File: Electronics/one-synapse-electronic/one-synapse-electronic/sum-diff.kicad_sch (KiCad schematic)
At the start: 25 parts, among them J2 Axon, J3 Axon, U2 MCP6004

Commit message: WIP
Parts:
- J2, J3: footprint (none) -> Connector_PinSocket_2.54mm:PinSocket_1x08_P2.54mm_Vertical
- U2: footprint (none) -> Package_SO:HTSSOP-14-1EP_4.4x5mm_P0.65mm_EP3.4x5mm_Mask3x3.1mm
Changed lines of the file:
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@@
       (effects (font (size 1.27 1.27)))
     )
-    (property "Footprint" "" (at 151.13 120.65 0)
+    (property "Footprint" "Package_SO:HTSSOP-14-1EP_4.4x5mm_P0.65mm_EP3.4x5mm_Mask3x3.1mm" (at 151.13 120.65 0)
       (effects (font (size 1.27 1.27)) hide)
     )
@@
       (effects (font (size 1.27 1.27)))
     )
-    (property "Footprint" "" (at 179.07 54.61 0)
+    (property "Footprint" "Package_SO:HTSSOP-14-1EP_4.4x5mm_P0.65mm_EP3.4x5mm_Mask3x3.1mm" (at 179.07 54.61 0)
       (effects (font (size 1.27 1.27)) hide)
     )
@@
       (effects (font (size 1.27 1.27)) (justify left))
     )
-    (property "Footprint" "" (at 214.63 67.31 0)
+    (property "Footprint" "Connector_PinSocket_2.54mm:PinSocket_1x08_P2.54mm_Vertical" (at 214.63 67.31 0)
       (effects (font (size 1.27 1.27)) hide)
     )
@@
       (effects (font (size 1.27 1.27)))
     )
-    (property "Footprint" "" (at 151.13 106.68 0)
+    (property "Footprint" "Package_SO:HTSSOP-14-1EP_4.4x5mm_P0.65mm_EP3.4x5mm_Mask3x3.1mm" (at 151.13 106.68 0)
       (effects (font (size 1.27 1.27)) hide)
     )
@@
       (effects (font (size 1.27 1.27)))
     )
-    (property "Footprint" "" (at 151.13 138.43 0)
+    (property "Footprint" "Package_SO:HTSSOP-14-1EP_4.4x5mm_P0.65mm_EP3.4x5mm_Mask3x3.1mm" (at 151.13 138.43 0)
       (effects (font (size 1.27 1.27)) hide)
     )
@@
       (effects (font (size 1.27 1.27)) (justify left))
     )
-    (property "Footprint" "" (at 214.63 44.45 0)
+    (property "Footprint" "Connector_PinSocket_2.54mm:PinSocket_1x08_P2.54mm_Vertical" (at 214.63 44.45 0)
       (effects (font (size 1.27 1.27)) hide)
     )
@@
       (effects (font (size 1.27 1.27)))
     )
-    (property "Footprint" "" (at 151.13 52.07 0)
-      (effects (font (size 1.27 1.27)) hide)
-    )
+    (property "Footprint" "Package_SO:HTSSOP-14-1EP_4.4x5mm_P0.65mm_EP3.4x5mm_Mask3x3.1mm" (at 151.13 52.07 0)
+      (effects (font (size 1.27 1.27)) hide)
+    )

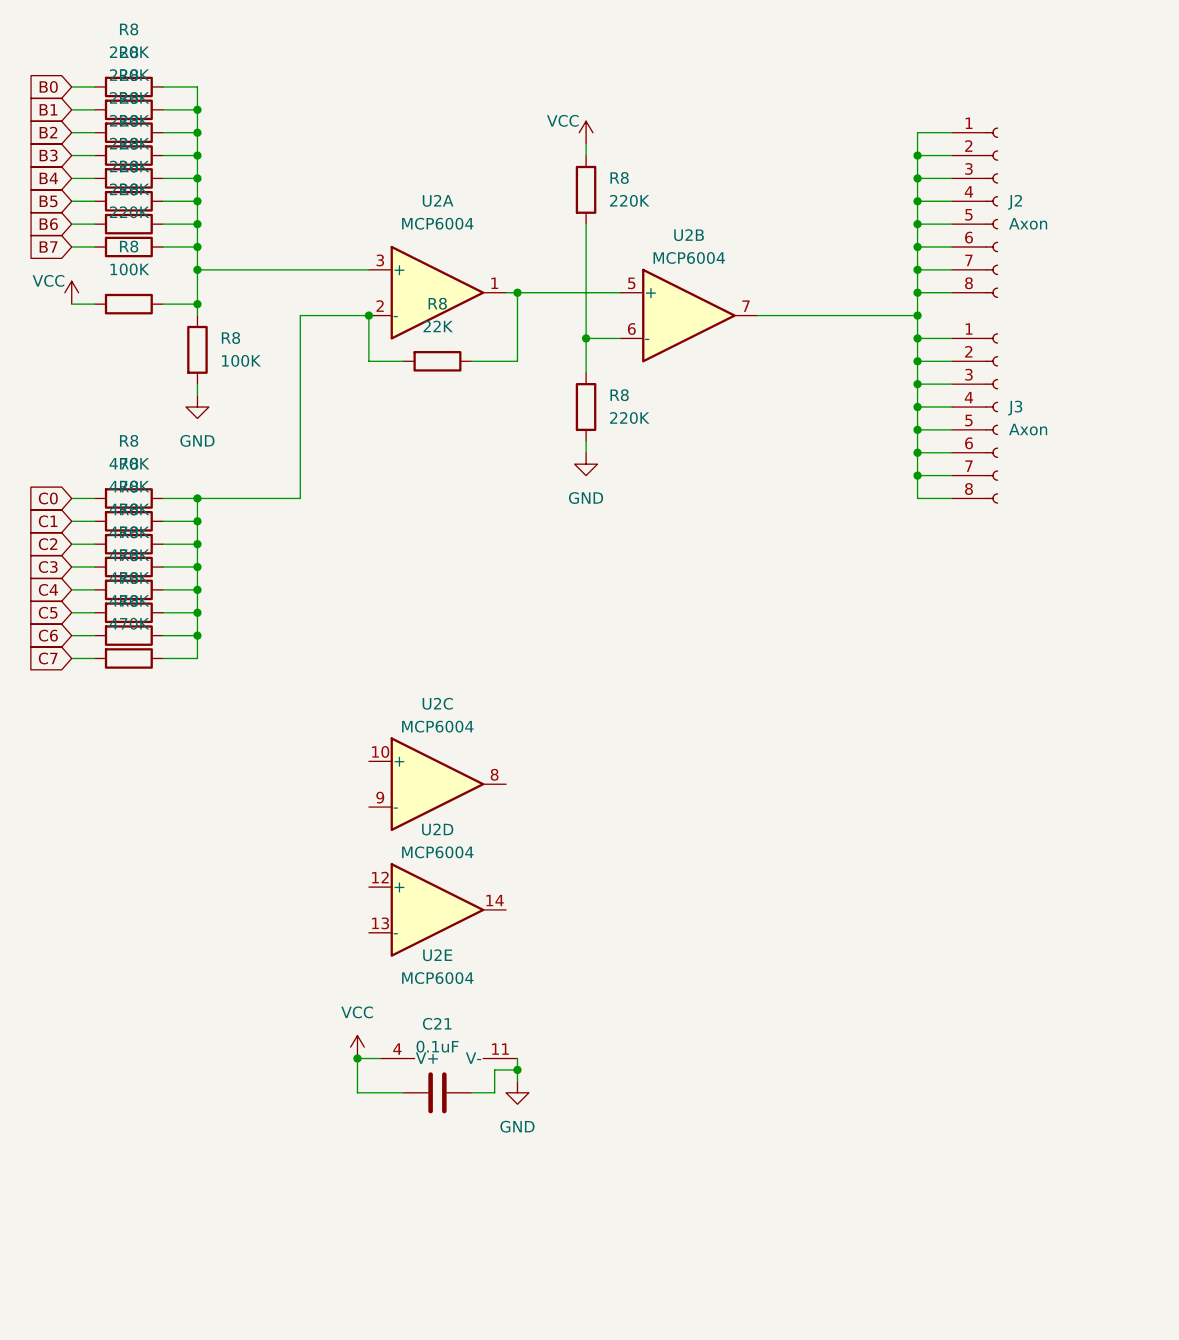
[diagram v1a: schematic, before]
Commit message: WIP. Added combiner i/o.
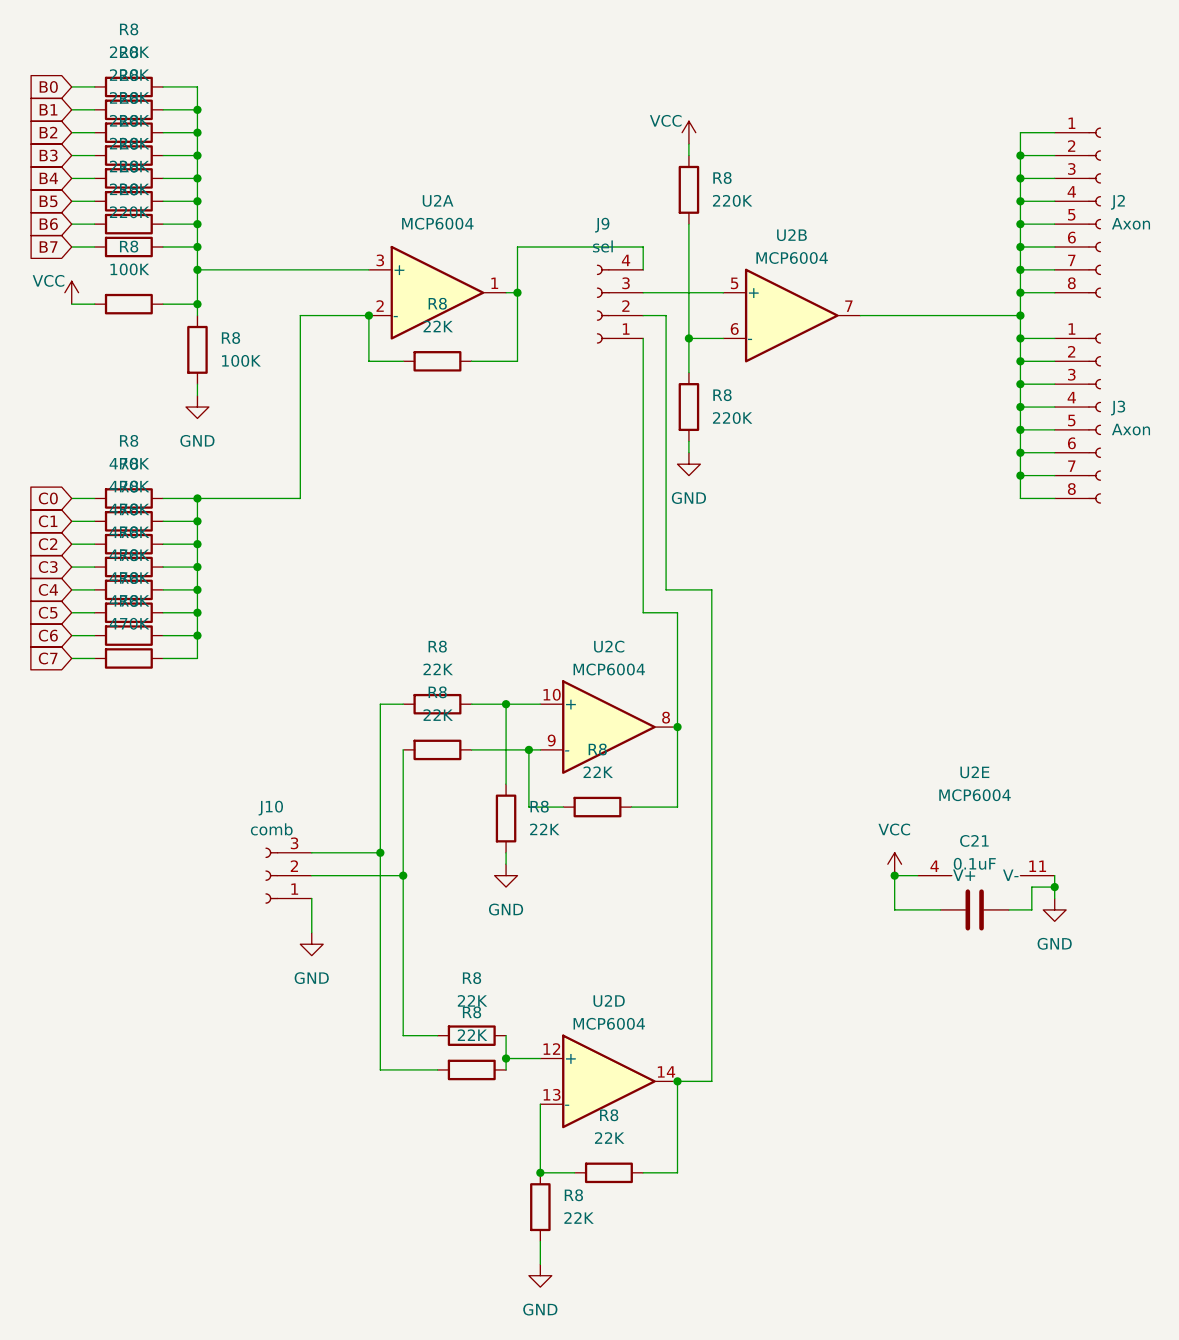
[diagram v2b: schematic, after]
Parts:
- added J10: comb, Connector_PinSocket_2.54mm:PinSocket_1x03_P2.54mm_Vertical, symbol Connector:Conn_01x03_Socket
- added J9: sel, Connector_PinSocket_2.54mm:PinSocket_1x04_P2.54mm_Vertical, symbol Connector:Conn_01x04_Socket
- added R8 (x8): 22K, Resistor_SMD:R_0805_2012Metric, symbol Device:R
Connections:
- net GND: now also J10.1 (Pin_1), R8.2, R8.2
- net at U2.12 (+): now also R8.1, R8.1
- net at U2.13 (-): now also R8.1, R8.2
- net at U2.14: now also J9.2 (Pin_2), R8.1
- net at R8.1, U2.1: now also J9.4 (Pin_4); no longer U2.5 (+)
- net at U2.10 (+): now also R8.1, R8.1
- net at U2.8: now also J9.1 (Pin_1), R8.1
- net at U2.9 (-): now also R8.1, R8.2
- new net: J9.3 (Pin_3), U2.5 (+)
- new net: J10.2 (Pin_2), R8.2, R8.2
- new net: J10.3 (Pin_3), R8.2, R8.2
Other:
- moved on the sheet: C21, J2, J3, R8, U2B, U2C, U2D, U2E
